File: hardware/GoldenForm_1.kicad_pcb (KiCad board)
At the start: 4 copper layers, 59.7 x 46.1 mm, 67 parts, among them IC1 UVLO, J1 1140084168, J2 Conn_01x02_Pin, J3 USB4105-GF-A, J4 Conn_01x04_Pin, J5 Conn_01x02_Pin, U1 ESP32-S3-WROOM-1, U2 BNO055, U3 Buck_Boost, U4 AO3400A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

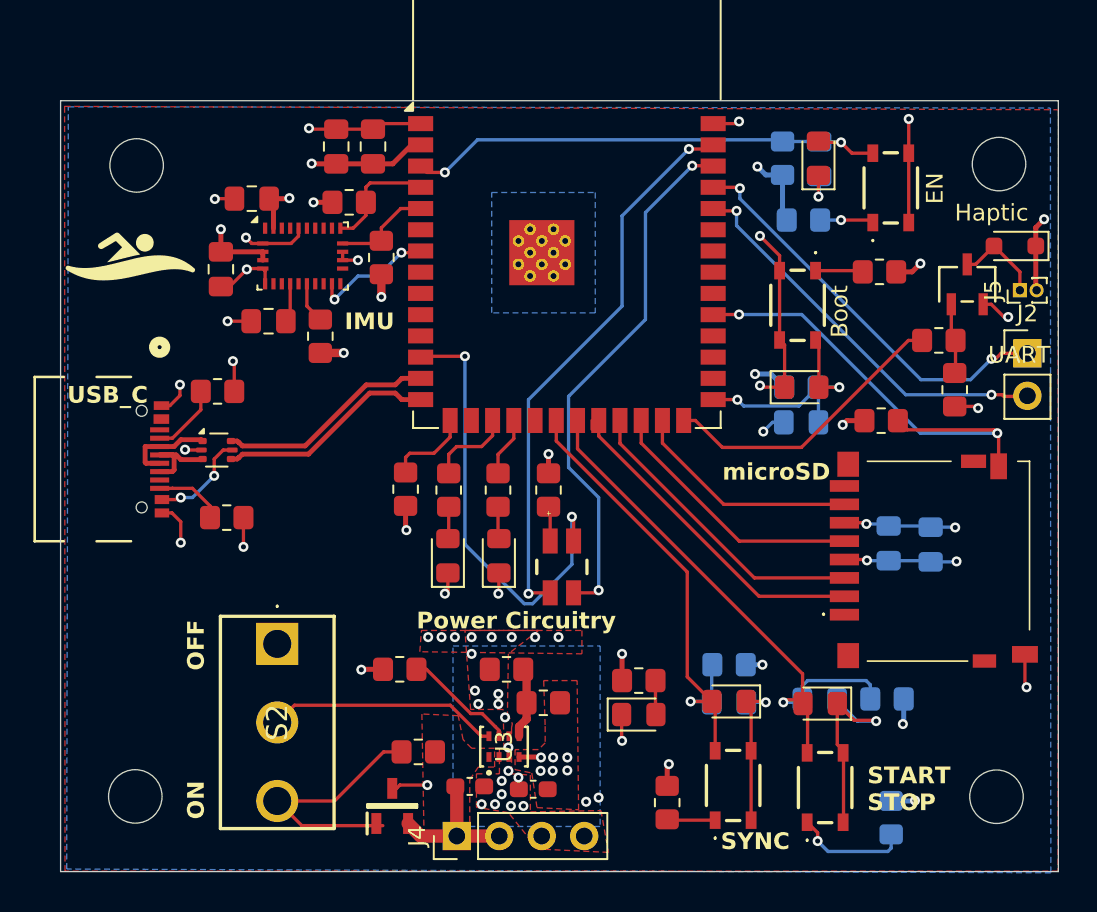
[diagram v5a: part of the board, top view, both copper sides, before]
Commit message: added shield res, and ext button headers
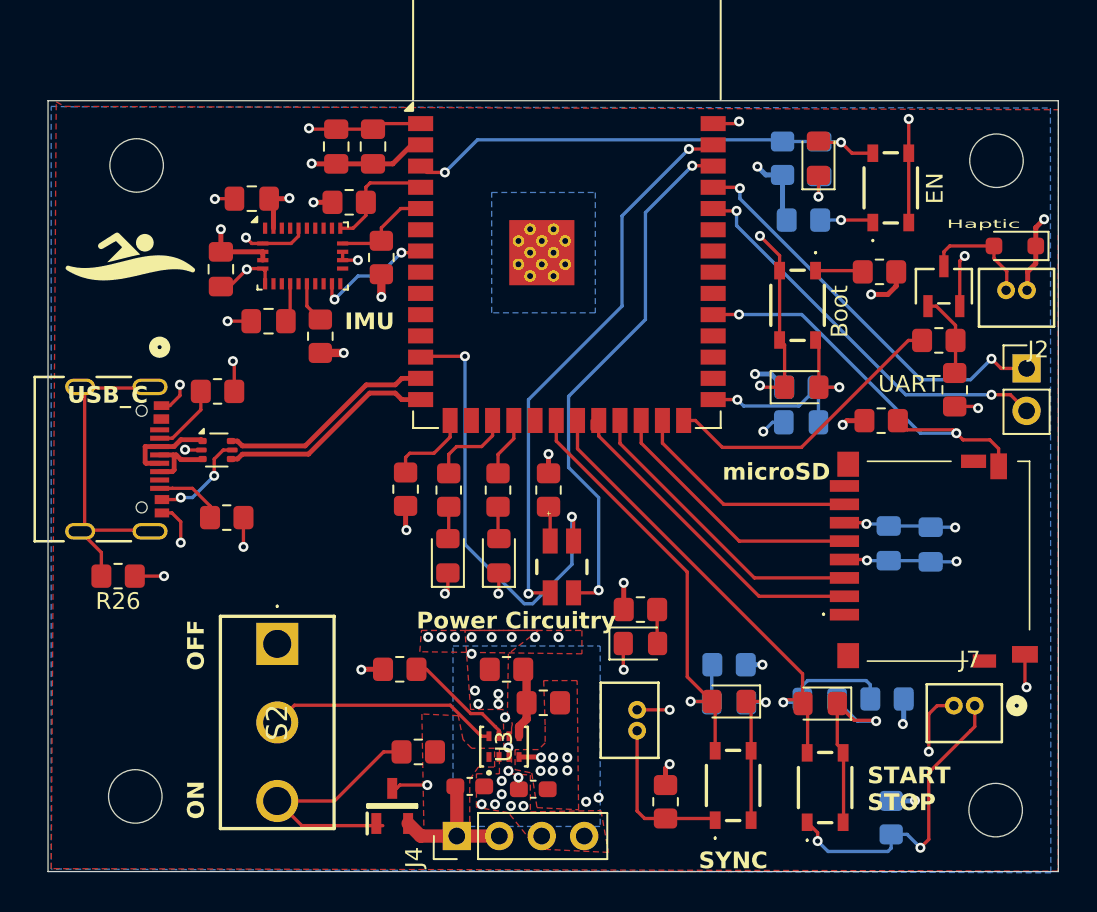
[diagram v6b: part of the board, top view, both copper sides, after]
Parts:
- added J6: 530470210, MyFootprints:CONN02_530470210_MOL, F.Cu at (102.3, 88.0)
- added J7: 530470210, MyFootprints:CONN02_530470210_MOL, F.Cu at (122.5, 86.5)
- added R26: 1M, Resistor_SMD:R_0805_2012Metric_Pad1.20x1.40mm_HandSolder, F.Cu at (71.2, 78.8)
- J5: value Conn_01x02_Pin -> 530470210; footprint Connector_PinHeader_1.00mm:PinHeader_1x02_P1.00mm_Vertical -> MyFootprints:CONN02_530470210_MOL
- moved D7 4.25 mm to (102.5, 82.8)
- moved R19 4.25 mm to (102.5, 80.8)
- moved U4 1.40 mm to (120.7, 61.4)
- moved J2 0.90 mm to (125.6, 66.3)
- moved REF** 0.80 mm to (123.8, 92.8)
- moved J5 0.42 mm to (125.6, 61.6), turned to 0 degrees
- moved REF** 0.25 mm to (123.8, 53.9)
- moved R21 0.11 mm to (104.0, 92.2)
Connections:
- J3 pad A6: USB_D+ -> D+
- J3 pad A7: USB_D- -> D-
- J3 pad B6: USB_D+ -> D+
- J3 pad B7: USB_D- -> D-
- J5 pad 1: Net-(D9-A) -> V_DD
- J5 pad 2: V_DD -> Net-(D9-A)
- U5 pad 1: USB_D- -> D-
- U5 pad 3: USB_D+ -> D+
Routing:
- net SHIELD: track 0.00 -> 19.8 mm
- net Net-(S4-NO_1): track 6.95 -> 18.9 mm, vias 1 -> 2
- net GND: track 92.7 -> 101.6 mm, vias 53 -> 56
- net Net-(S5-NO_1): track 2.89 -> 9.70 mm
- net D-: track 0.00 -> 5.47 mm
- net USB_D-: track 18.9 -> 13.4 mm
- net USB_D+: track 18.8 -> 13.4 mm
- net D+: track 0.00 -> 4.53 mm
- net SD_DETECT: track 28.2 -> 25.3 mm
- net Net-(D9-A): track 5.35 -> 6.97 mm
- net Net-(U4-G): track 4.24 -> 5.35 mm
- net V_DD: track 51.0 -> 52.1 mm
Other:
- board size 59.7 x 46.1 mm -> 60.4 x 46.1 mm

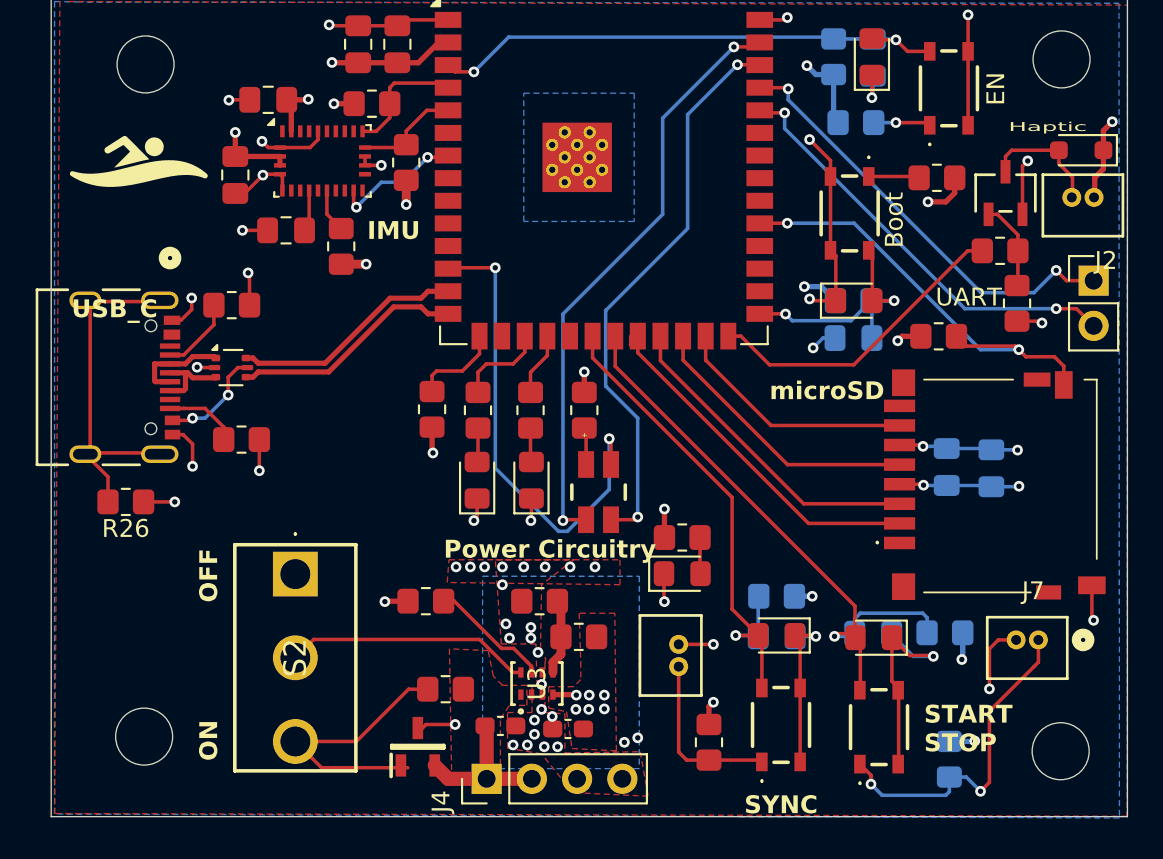
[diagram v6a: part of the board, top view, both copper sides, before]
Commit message: minor silkscreen changes
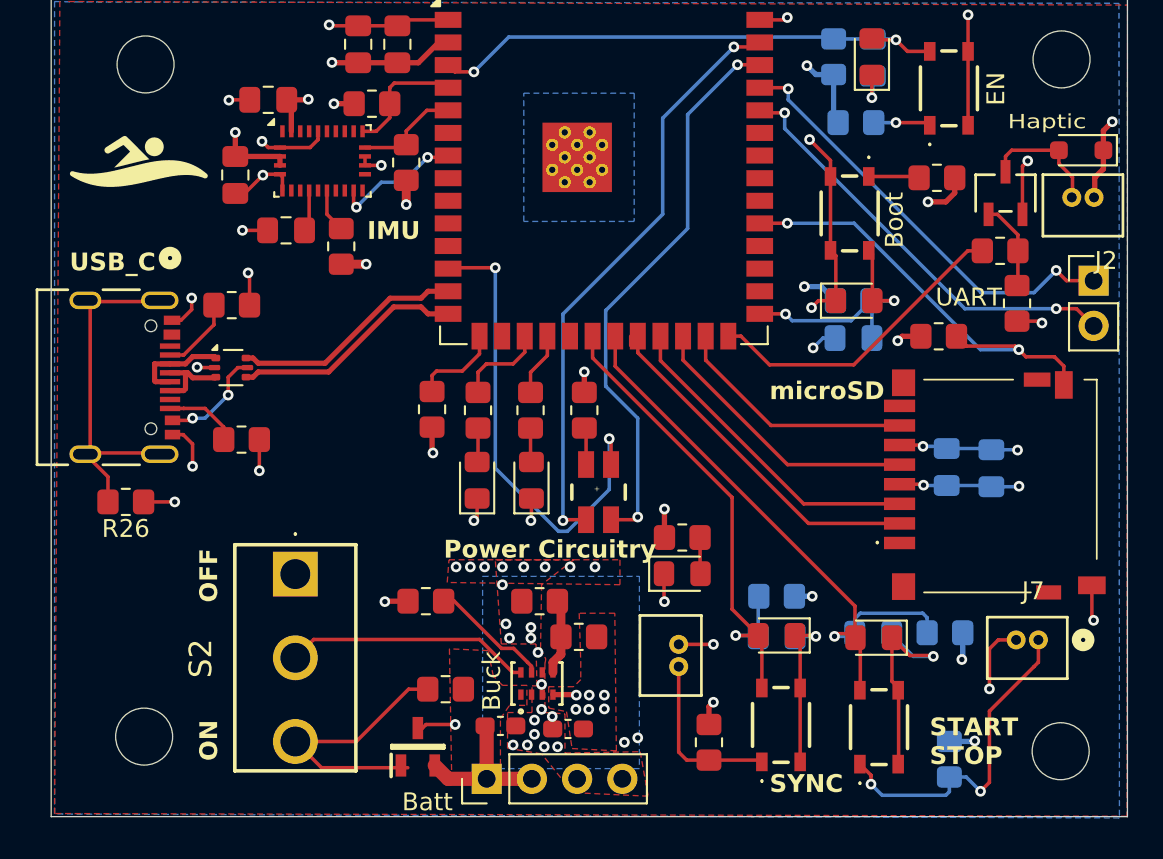
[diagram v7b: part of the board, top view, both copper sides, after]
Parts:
- renumbered J4 to Batt, U3 to Buck

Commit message: final PCB
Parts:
- removed R10, R14, R21, R9: 10k, Resistor_SMD:R_0805_2012Metric_Pad1.20x1.40mm_HandSolder
- moved J7 6.62 mm to (118.8, 92.0), turned to -90 degrees
- moved J6 4.25 mm to (103.8, 92.0)
- moved C12 0.35 mm to (113.2, 86.5)
- renumbered Batt to J4, Buck to U3
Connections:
- S1 pad 1: Net-(S1-NO_1) -> unconnected-(S1-NO_1-Pad1)
- S3 pad 1: Net-(S3-NO_1) -> unconnected-(S3-NO_1-Pad1)
- U1 pad 10: unconnected-(U1-IO17-Pad10) -> IO17
- U1 pad 11: unconnected-(U1-IO18-Pad11) -> HAPTIC
- U1 pad 26: HAPTIC -> unconnected-(U1-IO45-Pad26)
- U1 pad 8: unconnected-(U1-IO15-Pad8) -> IO15
- U1 pad 9: unconnected-(U1-IO16-Pad9) -> IO16
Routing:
- net IO16: track 0.00 -> 21.3 mm, vias 0 -> 2
- net IO15: track 0.00 -> 20.9 mm, vias 0 -> 2
- net IO17: track 0.00 -> 15.2 mm, vias 0 -> 2
- net HAPTIC: track 17.6 -> 32.1 mm, vias 0 -> 2
- net Net-(S4-NO_1): track 18.9 -> 9.65 mm, vias 2 -> 0
- net V_DD: track 52.1 -> 44.0 mm, vias 27 -> 24
- net Net-(S5-NO_1): track 9.70 -> 4.37 mm
- net Net-(S1-NO_1): track 3.21 -> 0.00 mm, vias 1 -> 0
- net Net-(S3-NO_1): track 2.86 -> 0.00 mm
- net GND: track 101.6 -> 101.0 mm, vias 56 -> 54
